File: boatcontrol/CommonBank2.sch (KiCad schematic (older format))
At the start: 23 parts, among them J5101 Conn_01x01_Male, J5102 TBP01R2W-508-08BE, J5103 Conn_01x01_Male, J5104 TBL008V-1000-02BE, J5105 TBP01R2W-508-08BE, J5106 Conn_01x01_Male, J5107 Conn_01x01_Male, J5108 TBL008V-1000-02BE, Q5101 IRF9510PBF-BE3, U5101 MCP23017-E/SP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

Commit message: Bottom done
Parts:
- removed Q5101: IRF9510PBF-BE3, Package_TO_SOT_THT:TO-220-3_Vertical, symbol BoatControl:IPP_B_I80P03
- added Q5101: IPP120P04P4L-03, Package_TO_SOT_THT:TO-220-3_Vertical, symbol BoatControl:IPP120P04P4L-03
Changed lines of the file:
@@
 	4300 1450 5200 1450
-$Comp
-L BoatControl:IPP_B_I80P03 Q?
-U 1 1 6329968F
-P 8300 6100
-AR Path="/6329968F" Ref="Q?"  Part="1"
-AR Path="/D16552B4/6329968F" Ref="Q?"  Part="1"
-AR Path="/D1BB8DB4/6329968F" Ref="Q5101"  Part="1"
-F 0 "Q5101" V 8150 5900 50  0000 L CNN
-F 1 "IRF9510PBF-BE3" V 8450 5750 50  0000 L CNN
-F 2 "Package_TO_SOT_THT:TO-220-3_Vertical" H 8300 6100 50  0001 C CNN
-F 3 "https://www.vishay.com/docs/91072/91072.pdf" H 8300 6100 50  0001 C CNN
-F 4 "P-Channel 100V 4A (Tc) 43W (Tc) Through Hole TO-220AB" H 8300 6100 50  0001 C CNN "Description"
-F 5 "Vishay Siliconix" H 8300 6100 50  0001 C CNN "Manufacturer"
-	1    8300 6100
-	0    1    1    0
-$EndComp
 $Comp
 L power:GND #PWR?
@@
 Wire Wire Line
 	7700 6100 8100 6100
+$Comp
+L BoatControl:IPP120P04P4L-03 Q5101
+U 1 1 5FED44A8
+P 8300 6100
+F 0 "Q5101" V 7950 6100 50  0000 C CNN
+F 1 "IPP120P04P4L-03" V 8450 6100 50  0000 C CNN
+F 2 "Package_TO_SOT_THT:TO-220-3_Vertical" H 7950 6650 50  0001 C CNN
+F 3 "https://www.infineon.com/dgdl/Infineon-I80P03P4L_04-DS-v01_01-en.pdf?folderId=db3a304314dca3890114ef902baa05f9&fileId=db3a30431ddc9372011e07e95eb827d7&ack=t" H 8300 6100 50  0001 C CNN
+F 4 "P-Channel 30V 80A (Tc) 137W (Tc) Through Hole PG-TO220-3-1" H 8150 6750 50  0001 C CNN "Description"
+F 5 "OptiMOS" H 8900 6400 50  0001 C CNN "Series"
+F 6 "Infineon Technologies" H 8800 6500 50  0001 C CNN "Infineon Technologies"
+	1    8300 6100
+	0    1    1    0
+$EndComp
 $EndSCHEMATC

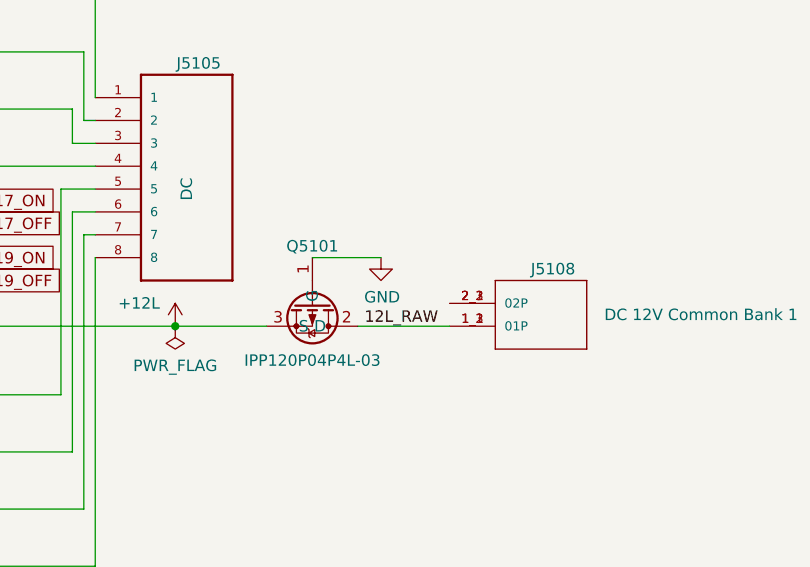
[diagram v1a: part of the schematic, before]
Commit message: Fix polarity mosfets
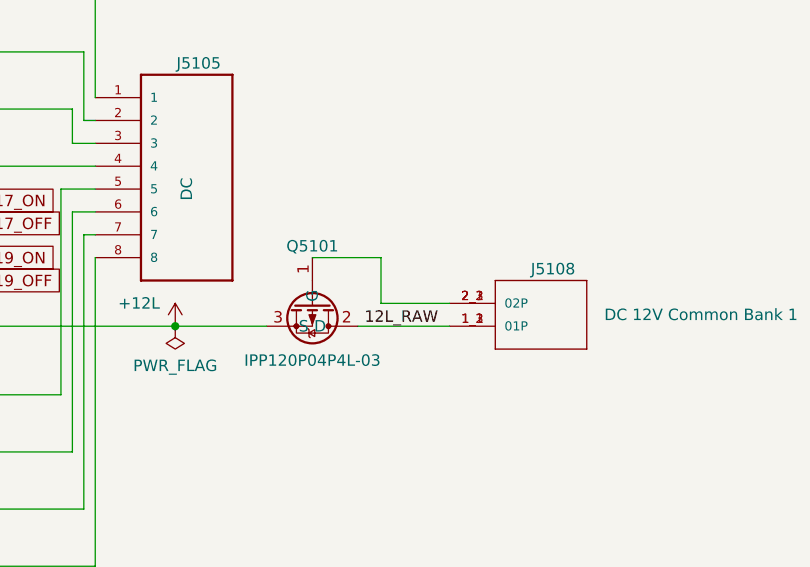
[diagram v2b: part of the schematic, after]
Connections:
- net GND: no longer Q5101.1 (G)
- net at J5108.2_1 (02P), J5108.2_2 (02P), J5108.2_3 (02P): now also Q5101.1 (G)
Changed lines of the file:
@@
 Wire Wire Line
 	4300 1450 5200 1450
-$Comp
-L power:GND #PWR?
-U 1 1 623D507C
-P 8600 5800
-AR Path="/D16552B4/623D507C" Ref="#PWR?"  Part="1"
-AR Path="/D1BB8DB4/623D507C" Ref="#PWR05105"  Part="1"
-F 0 "#PWR05105" H 8600 5550 50  0001 C CNN
-F 1 "GND" H 8605 5627 50  0000 C CNN
-F 2 "" H 8600 5800 50  0001 C CNN
-F 3 "" H 8600 5800 50  0001 C CNN
-	1    8600 5800
-	1    0    0    -1
-$EndComp
 Wire Wire Line
 	8300 5800 8600 5800
@@
 	0    1    1    0
 $EndComp
+Wire Wire Line
+	8600 5800 8600 6000
+Wire Wire Line
+	8600 6000 8900 6000
 $EndSCHEMATC

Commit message: Add reverse/AC/DC polarity indicators
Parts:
- added D? (x2): 20mA R/G Bicolor, LED_THT:LED_D5.0mm, symbol Device:LED_Dual_2pin
- added R? (x2): 680Ω, Resistor_THT:R_Axial_DIN0207_L6.3mm_D2.5mm_P7.62mm_Horizontal, symbol Device:R_Small
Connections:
- net 12L_RAW: now also R?.2
- net AC: now also R?.2
- net at J5108.2_1 (02P), J5108.2_2 (02P), J5108.2_3 (02P)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: now also D?.2 (AK)
- net at J5104.2_1 (02P), J5104.2_2 (02P), J5104.2_3 (02P): now also D?.2 (AK)
- new net: D?.1 (KA), R?.1 (x2)
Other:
- moved on the sheet: J5104, J5108

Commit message: Fix AC resistor for polarity indicator
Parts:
- R?: value 680Ω -> 12KΩ; Description 680 Ohms ±1% 0.6W Through Hole Resistor Axial Metal Film -> 12 kOhms ±5% 0.5W, 1/2W Through Hole Resistor Axial Flame P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; Product LR1F680R -> ROX05SJ12K‎
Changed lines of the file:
@@
 AR Path="/D1BB8DB4/60113E2D" Ref="R?"  Part="1"
 F 0 "R?" H 8900 2150 50  0000 C CNN
-F 1 "680Ω" H 8800 2400 50  0000 C CNN
+F 1 "12KΩ" H 8800 2400 50  0000 C CNN
 F 2 "Resistor_THT:R_Axial_DIN0207_L6.3mm_D2.5mm_P7.62mm_Horizontal" H 8800 2250 50  0001 C CNN
-F 3 "https://www.te.com/commerce/DocumentDelivery/DDEController?Action=srchrtrv&DocNm=1773241&DocType=DS&DocLang=English" H 8800 2250 50  0001 C CNN
-F 4 "LR1F680R" H 8800 2250 50  0001 C CNN "Product"
+F 3 "" H 8800 2250 50  0001 C CNN
+F 4 "ROX05SJ12K‎" H 8800 2250 50  0001 C CNN "Product"
 F 5 "TE Connectivity" H 8800 2250 50  0001 C CNN "Manufacturer"
-F 6 "680 Ohms ±1% 0.6W Through Hole Resistor Axial Metal Film" H 8800 2250 50  0001 C CNN "Description"
+F 6 "12 kOhms ±5% 0.5W, 1/2W Through Hole Resistor Axial Flame Proof, Pulse Withstanding, Safety Metal Oxide Film" H 8800 2250 50  0001 C CNN "Description"
 	1    8800 2250
 	1    0    0    -1

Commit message: Fix LED resistors
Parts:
- gave numbers to parts that had none: 4
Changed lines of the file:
@@
 AR Path="/D1BB8DB4/5F75E923/60474911/600A5AB3" Ref="D?"  Part="1"
 AR Path="/D16552B4/600A5AB3" Ref="D?"  Part="1"
-AR Path="/D1BB8DB4/600A5AB3" Ref="D?"  Part="1"
-F 0 "D?" H 8950 5700 50  0000 C CNN
+AR Path="/D1BB8DB4/600A5AB3" Ref="D5102"  Part="1"
+F 0 "D5102" H 8950 5700 50  0000 C CNN
 F 1 "20mA R/G Bicolor" H 9150 6200 50  0000 C CNN
 F 2 "LED_THT:LED_D5.0mm" H 9200 5850 50  0001 C CNN
@@
 P 8900 5950
 AR Path="/D16552B4/600A5ABC" Ref="R?"  Part="1"
-AR Path="/D1BB8DB4/600A5ABC" Ref="R?"  Part="1"
-F 0 "R?" H 9000 5850 50  0000 C CNN
+AR Path="/D1BB8DB4/600A5ABC" Ref="R5102"  Part="1"
+F 0 "R5102" H 9000 5850 50  0000 C CNN
 F 1 "680Ω" H 8900 6100 50  0000 C CNN
 F 2 "Resistor_THT:R_Axial_DIN0207_L6.3mm_D2.5mm_P7.62mm_Horizontal" H 8900 5950 50  0001 C CNN
@@
 AR Path="/D1BB8DB4/5F75E923/60474911/60113E24" Ref="D?"  Part="1"
 AR Path="/D16552B4/60113E24" Ref="D?"  Part="1"
-AR Path="/D1BB8DB4/60113E24" Ref="D?"  Part="1"
-F 0 "D?" H 8850 2000 50  0000 C CNN
+AR Path="/D1BB8DB4/60113E24" Ref="D5101"  Part="1"
+F 0 "D5101" H 8850 2000 50  0000 C CNN
 F 1 "20mA R/G Bicolor" H 9050 2500 50  0000 C CNN
 F 2 "LED_THT:LED_D5.0mm" H 9100 2150 50  0001 C CNN
@@
 P 8800 2250
 AR Path="/D16552B4/60113E2D" Ref="R?"  Part="1"
-AR Path="/D1BB8DB4/60113E2D" Ref="R?"  Part="1"
-F 0 "R?" H 8900 2150 50  0000 C CNN
+AR Path="/D1BB8DB4/60113E2D" Ref="R5101"  Part="1"
+F 0 "R5101" H 8900 2150 50  0000 C CNN
 F 1 "12KΩ" H 8800 2400 50  0000 C CNN
 F 2 "Resistor_THT:R_Axial_DIN0207_L6.3mm_D2.5mm_P7.62mm_Horizontal" H 8800 2250 50  0001 C CNN

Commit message: Figure out wiring cluster
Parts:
- added JP5109, JP5110: Jumper_NO_Small, Connector_PinHeader_2.54mm:PinHeader_1x02_P2.54mm_Vertical, symbol Device:Jumper_NO_Small
- Q5101: Note (none) -> Optional, can be substituded with shunt; Purpose (none) -> Reverse Polarity (Voltage) Protection
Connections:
- net at J5108.2_1 (02P), J5108.2_2 (02P), J5108.2_3 (02P)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: now also JP5110.1; no longer D5102.2 (AK)
- net at J5104.2_1 (02P), J5104.2_2 (02P), J5104.2_3 (02P): now also JP5109.1; no longer D5101.2 (AK)
- new net: D5102.2 (AK), JP5110.2
- new net: D5101.2 (AK), JP5109.2
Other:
- note added: "It's safe to run AC up to 277V 50/60hz and DC up to 24V on this circuit even though it's marked AC.\nThe main difference between this and the DC specific circuits is track spacing and lack of any polarity protection."
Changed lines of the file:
@@
-$EndComp
-$Comp
-L BoatControl:TBL008V-1000-02BE J?
-U 1 1 D24C1AB1
-P 10050 2300
-AR Path="/D24C1AB1" Ref="J?"  Part="1"
-AR Path="/D1BB8DB4/D24C1AB1" Ref="J5104"  Part="1"
-F 0 "J5104" H 10250 2150 50  0000 R CNN
-F 1 "TBL008V-1000-02BE" H 10450 2150 50  0001 R CNN
-F 2 "CUI_TBL008V-1000-02BE" H 10050 2300 50  0001 L BNN
-F 3 "CUI" H 10050 2300 50  0001 L BNN
-F 4 "AC 230V Common Bank" H 10050 2600 50  0000 C CNN "Type"
-	1    10050 2300
-	1    0    0    1
 $EndComp
 $Comp
@@
 Wire Wire Line
 	9750 5600 8300 5600
-Wire Wire Line
-	9750 5850 9500 5850
 $Comp
 L BoatControl:IPP120P04P4L-03 Q5101
 U 1 1 5FED44A8
 P 8300 6100
+AR Path="/D1BB8DB4/5FED44A8" Ref="Q5101"  Part="1"
+AR Path="/D16552B4/5FA17F38/5FED44A8" Ref="Q5101"  Part="1"
 F 0 "Q5101" V 8100 6250 50  0000 C CNN
 F 1 "IPP120P04P4L-03" V 8450 6100 50  0000 C CNN
@@
 F 5 "OptiMOS" H 8900 6400 50  0001 C CNN "Series"
 F 6 "Infineon Technologies" H 8800 6500 50  0001 C CNN "Infineon Technologies"
+F 7 "Reverse Polarity (Voltage) Protection" H 7450 5950 50  0000 C CNN "Purpose"
+F 8 "Optional, can be substituded with shunt" H 7250 6050 50  0000 C CNN "Note"
 	1    8300 6100
 	0    1    1    0
 $EndComp
-Wire Wire Line
-	9750 6000 9750 5850
-Wire Wire Line
-	9750 5850 9750 5600
-Connection ~ 9750 5850
 Wire Wire Line
 	8300 5600 8300 5800
@@
 	8800 2400 9650 2400
 Wire Wire Line
-	9650 2150 9400 2150
-Wire Wire Line
 	9650 2300 9650 2150
 Wire Wire Line
 	8150 2400 8800 2400
 Connection ~ 8150 2400
+$Comp
+L Device:Jumper_NO_Small JP?
+U 1 1 61788453
+P 9600 5850
+AR Path="/61788453" Ref="JP?"  Part="1"
+AR Path="/D16552B4/61788453" Ref="JP?"  Part="1"
+AR Path="/D1BB8DB4/61788453" Ref="JP5110"  Part="1"
+F 0 "JP5110" H 9600 5950 50  0000 C CNN
+F 1 "Jumper_NO_Small" H 9650 5750 50  0001 C CNN
+F 2 "Connector_PinHeader_2.54mm:PinHeader_1x02_P2.54mm_Vertical" H 9600 5850 50  0001 C CNN
+F 3 "~" H 9600 5850 50  0001 C CNN
+	1    9600 5850
+	-1   0    0    1
+$EndComp
+Wire Wire Line
+	9750 5600 9750 5850
+Wire Wire Line
+	9700 5850 9750 5850
+Connection ~ 9750 5850
+Wire Wire Line
+	9750 5850 9750 6000
+$Comp
+L Device:Jumper_NO_Small JP?
+U 1 1 617AACB3
+P 9500 2150
+AR Path="/617AACB3" Ref="JP?"  Part="1"
+AR Path="/D16552B4/617AACB3" Ref="JP?"  Part="1"
+AR Path="/D1BB8DB4/617AACB3" Ref="JP5109"  Part="1"
+F 0 "JP5109" H 9500 2250 50  0000 C CNN
+F 1 "Jumper_NO_Small" H 9550 2050 50  0001 C CNN
+F 2 "Connector_PinHeader_2.54mm:PinHeader_1x02_P2.54mm_Vertical" H 9500 2150 50  0001 C CNN
+F 3 "~" H 9500 2150 50  0001 C CNN
+	1    9500 2150
+	-1   0    0    1
+$EndComp
+Wire Wire Line
+	9600 2150 9650 2150
+Text Notes 7400 1100 0    50   ~ 0
+It's safe to run AC up to 277V 50/60hz and DC up to 24V on this circuit even though it's marked AC.\nThe main difference between this and the DC specific circuits  is track spacing and lack of any polarity protection.
+$Comp
+L BoatControl:TBL008V-1000-02BE J?
+U 1 1 D24C1AB1
+P 10050 2300
+AR Path="/D24C1AB1" Ref="J?"  Part="1"
+AR Path="/D1BB8DB4/D24C1AB1" Ref="J5104"  Part="1"
+F 0 "J5104" H 10250 2150 50  0000 R CNN
+F 1 "TBL008V-1000-02BE" H 10450 2150 50  0001 R CNN
+F 2 "CUI_TBL008V-1000-02BE" H 10050 2300 50  0001 L BNN
+F 3 "CUI" H 10050 2300 50  0001 L BNN
+F 4 "AC 230V Common Bank" H 10050 2600 50  0000 C CNN "Type"
+	1    10050 2300
+	1    0    0    1
+$EndComp
 $EndSCHEMATC

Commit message: Add remaining bypass capacitors
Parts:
- C5101, C5103: value 10uF -> 10μF; footprint Capacitor_THT:CP_Radial_D8.0mm_P5.00mm -> Capacitor_THT:C_Disc_D7.5mm_W5.0mm_P5.00mm; symbol Device:CP1_Small -> Device:C_Small
- C5102, C5104: value 0.1uF -> 0.1μF; footprint Capacitor_THT:CP_Radial_D8.0mm_P5.00mm -> Capacitor_THT:C_Disc_D7.5mm_W5.0mm_P5.00mm; symbol Device:CP1_Small -> Device:C_Small
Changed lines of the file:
@@
 Wire Wire Line
 	2150 6200 2150 5000
-Wire Wire Line
-	2150 5000 3350 5000
 Connection ~ 2150 6200
 Wire Wire Line
@@
 Wire Wire Line
 	2150 2050 2150 850
-Wire Wire Line
-	2150 850  3350 850
 Connection ~ 2150 2050
 Wire Wire Line
@@
 AR Path="/D1BB8DB4/D2B4FF02" Ref="#PWR05104"  Part="1"
 F 0 "#PWR05104" H 3350 4850 50  0001 C CNN
-F 1 "+5V" H 3500 5050 50  0000 C CNN
+F 1 "+5V" V 3350 5200 50  0000 C CNN
 F 2 "" H 3350 5000 50  0001 C CNN
 F 3 "" H 3350 5000 50  0001 C CNN
 	1    3350 5000
-	1    0    0    -1
+	0    1    1    0
 $EndComp
 Connection ~ 3350 850
@@
 AR Path="/D1BB8DB4/D1AAA338" Ref="#PWR05101"  Part="1"
 F 0 "#PWR05101" H 3350 700 50  0001 C CNN
-F 1 "+5V" H 3500 900 50  0000 C CNN
+F 1 "+5V" V 3350 1050 50  0000 C CNN
 F 2 "" H 3350 850 50  0001 C CNN
 F 3 "" H 3350 850 50  0001 C CNN
 	1    3350 850
-	1    0    0    -1
+	0    1    1    0
 $EndComp
 $Comp
@@
 	6550 6300 6550 6550
 $Comp
-L Device:CP1_Small C?
+L Device:C_Small C?
 U 1 1 618DAE42
-P 700 1850
+P 3000 750
 AR Path="/618DAE42" Ref="C?"  Part="1"
 AR Path="/D1BB8DB4/618DAE42" Ref="C5101"  Part="1"
-F 0 "C5101" V 650 1600 50  0000 L CNN
-F 1 "10uF" H 791 1805 50  0001 L CNN
-F 2 "Capacitor_THT:CP_Radial_D8.0mm_P5.00mm" H 700 1850 50  0001 C CNN
-F 3 "https://www.mouser.ca/datasheet/2/212/KEM_C1050_GOLDMAX_X7R-1518817.pdf" H 700 1850 50  0001 C CNN
-F 4 "Kemet" H 700 1850 50  0001 C CNN "Manufacturer"
-F 5 "C322C106K3R5TA" V 700 1850 50  0001 C CNN "Model"
-	1    700  1850
-	1    0    0    -1
-$EndComp
-$Comp
-L Device:CP1_Small C?
+F 0 "C5101" H 2900 550 50  0000 L CNN
+F 1 "10μF" H 3091 705 50  0001 L CNN
+F 2 "Capacitor_THT:C_Disc_D7.5mm_W5.0mm_P5.00mm" H 3000 750 50  0001 C CNN
+F 3 "https://www.mouser.ca/datasheet/2/212/KEM_C1050_GOLDMAX_X7R-1518817.pdf" H 3000 750 50  0001 C CNN
+F 4 "Kemet" H 3000 750 50  0001 C CNN "Manufacturer"
+F 5 "C322C106K3R5TA" V 3000 750 50  0001 C CNN "Model"
+	1    3000 750
+	-1   0    0    1
+$EndComp
+$Comp
+L Device:C_Small C?
 U 1 1 618DAE4A
-P 900 1850
+P 3250 750
 AR Path="/618DAE4A" Ref="C?"  Part="1"
 AR Path="/D1BB8DB4/618DAE4A" Ref="C5102"  Part="1"
-F 0 "C5102" V 850 1600 50  0000 L CNN
-F 1 "0.1uF" H 991 1805 50  0001 L CNN
-F 2 "Capacitor_THT:CP_Radial_D8.0mm_P5.00mm" H 900 1850 50  0001 C CNN
-F 3 "https://www.mouser.ca/datasheet/2/212/KEM_C1050_GOLDMAX_X7R-1518817.pdf" H 900 1850 50  0001 C CNN
-F 4 "Kemet" H 900 1850 50  0001 C CNN "Manufacturer"
-F 5 "C320C104K3R5TA" V 900 1850 50  0001 C CNN "Model"
-	1    900  1850
-	1    0    0    -1
-$EndComp
-Wire Wire Line
-	700  1750 700  850
-Wire Wire Line
-	900  850  900  1750
-Wire Wire Line
-	700  1950 700  3050
-Wire Wire Line
-	900  1950 900  3050
-$Comp
-L Device:CP1_Small C?
+F 0 "C5102" H 3150 550 50  0000 L CNN
+F 1 "0.1μF" H 3341 705 50  0001 L CNN
+F 2 "Capacitor_THT:C_Disc_D7.5mm_W5.0mm_P5.00mm" H 3250 750 50  0001 C CNN
+F 3 "https://www.mouser.ca/datasheet/2/212/KEM_C1050_GOLDMAX_X7R-1518817.pdf" H 3250 750 50  0001 C CNN
+F 4 "Kemet" H 3250 750 50  0001 C CNN "Manufacturer"
+F 5 "C320C104K3R5TA" V 3250 750 50  0001 C CNN "Model"
+	1    3250 750
+	-1   0    0    1
+$EndComp
+$Comp
+L Device:C_Small C?
 U 1 1 618E7D21
-P 650 6000
+P 3000 4900
 AR Path="/618E7D21" Ref="C?"  Part="1"
 AR Path="/D1BB8DB4/618E7D21" Ref="C5103"  Part="1"
-F 0 "C5103" V 600 5750 50  0000 L CNN
-F 1 "10uF" H 741 5955 50  0001 L CNN
-F 2 "Capacitor_THT:CP_Radial_D8.0mm_P5.00mm" H 650 6000 50  0001 C CNN
-F 3 "https://www.mouser.ca/datasheet/2/212/KEM_C1050_GOLDMAX_X7R-1518817.pdf" H 650 6000 50  0001 C CNN
-F 4 "Kemet" H 650 6000 50  0001 C CNN "Manufacturer"
-F 5 "C322C106K3R5TA" V 650 6000 50  0001 C CNN "Model"
-	1    650  6000
-	1    0    0    -1
-$EndComp
-$Comp
-L Device:CP1_Small C?
+F 0 "C5103" H 2900 4700 50  0000 L CNN
+F 1 "10μF" H 3091 4855 50  0001 L CNN
+F 2 "Capacitor_THT:C_Disc_D7.5mm_W5.0mm_P5.00mm" H 3000 4900 50  0001 C CNN
+F 3 "https://www.mouser.ca/datasheet/2/212/KEM_C1050_GOLDMAX_X7R-1518817.pdf" H 3000 4900 50  0001 C CNN
+F 4 "Kemet" H 3000 4900 50  0001 C CNN "Manufacturer"
+F 5 "C322C106K3R5TA" V 3000 4900 50  0001 C CNN "Model"
+	1    3000 4900
+	-1   0    0    1
+$EndComp
+$Comp
+L Device:C_Small C?
 U 1 1 618E7D29
-P 850 6000
+P 3250 4900
 AR Path="/618E7D29" Ref="C?"  Part="1"
 AR Path="/D1BB8DB4/618E7D29" Ref="C5104"  Part="1"
-F 0 "C5104" V 800 5750 50  0000 L CNN
-F 1 "0.1uF" H 941 5955 50  0001 L CNN
-F 2 "Capacitor_THT:CP_Radial_D8.0mm_P5.00mm" H 850 6000 50  0001 C CNN
-F 3 "https://www.mouser.ca/datasheet/2/212/KEM_C1050_GOLDMAX_X7R-1518817.pdf" H 850 6000 50  0001 C CNN
-F 4 "Kemet" H 850 6000 50  0001 C CNN "Manufacturer"
-F 5 "C320C104K3R5TA" V 850 6000 50  0001 C CNN "Model"
-	1    850  6000
-	1    0    0    -1
-$EndComp
-Wire Wire Line
-	650  5900 650  5000
-Wire Wire Line
-	850  5000 850  5900
-Wire Wire Line
-	650  6100 650  7200
-Wire Wire Line
-	850  6100 850  7200
-Wire Wire Line
-	700  850  900  850
-Connection ~ 1100 850
-Connection ~ 900  850
-Wire Wire Line
-	900  850  1100 850
-Wire Wire Line
-	700  3050 900  3050
-Connection ~ 1500 3050
-Connection ~ 900  3050
-Wire Wire Line
-	900  3050 1500 3050
-Wire Wire Line
-	650  5000 850  5000
-Connection ~ 1100 5000
-Connection ~ 850  5000
-Wire Wire Line
-	850  5000 1100 5000
-Wire Wire Line
-	650  7200 850  7200
-Connection ~ 1500 7200
-Connection ~ 850  7200
-Wire Wire Line
-	850  7200 1500 7200
+F 0 "C5104" H 3150 4700 50  0000 L CNN
+F 1 "0.1μF" H 3341 4855 50  0001 L CNN
+F 2 "Capacitor_THT:C_Disc_D7.5mm_W5.0mm_P5.00mm" H 3250 4900 50  0001 C CNN
+F 3 "https://www.mouser.ca/datasheet/2/212/KEM_C1050_GOLDMAX_X7R-1518817.pdf" H 3250 4900 50  0001 C CNN
+F 4 "Kemet" H 3250 4900 50  0001 C CNN "Manufacturer"
+F 5 "C320C104K3R5TA" V 3250 4900 50  0001 C CNN "Model"
+	1    3250 4900
+	-1   0    0    1
+$EndComp
 Wire Wire Line
 	6550 5300 6550 6100
@@
 	1    0    0    1
 $EndComp
+$Comp
+L power:GND #PWR0196
+U 1 1 61D07DAF
+P 3250 650
+F 0 "#PWR0196" H 3250 400 50  0001 C CNN
+F 1 "GND" V 3255 522 50  0000 R CNN
+F 2 "" H 3250 650 50  0001 C CNN
+F 3 "" H 3250 650 50  0001 C CNN
+	1    3250 650
+	0    -1   -1   0
+$EndComp
+Wire Wire Line
+	3250 650  3000 650
+Wire Wire Line
+	3000 4800 3250 4800
+$Comp
+L power:GND #PWR0197
+U 1 1 61D70609
+P 3250 4800
+F 0 "#PWR0197" H 3250 4550 50  0001 C CNN
+F 1 "GND" V 3255 4672 50  0000 R CNN
+F 2 "" H 3250 4800 50  0001 C CNN
+F 3 "" H 3250 4800 50  0001 C CNN
+	1    3250 4800
+	0    -1   -1   0
+$EndComp
+Wire Wire Line
+	2150 850  3000 850
+Connection ~ 3000 850
+Wire Wire Line
+	3000 850  3250 850
+Connection ~ 3250 850
+Wire Wire Line
+	3250 850  3350 850
+Connection ~ 3250 650
+Wire Wire Line
+	2150 5000 3000 5000
+Connection ~ 3000 5000
+Wire Wire Line
+	3000 5000 3250 5000
+Connection ~ 3250 5000
+Wire Wire Line
+	3250 5000 3350 5000
+Connection ~ 3250 4800
 $EndSCHEMATC
